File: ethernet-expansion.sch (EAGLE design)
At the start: 22 parts, among them Q1 25MHz, U1 ENC28J60-SO

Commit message: Add center tap connection and interrupt connections
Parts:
- C10, C5, C7, C8, C9: value 100nF -> 0.1uF
- C4, C6: value 0.01uF -> 0.1uF
- R1, R2, R3, R4: value 50 -> 49.9
- R9: value 2K -> 2.32K
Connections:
- net +3V3: now also RJ1.P4
- net ETH_INT0: now also JP1.9
- net ETH_INT1: now also JP1.7
- net GND: now also RJ1.GND

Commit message: Started to route the connector
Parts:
- removed C3: 10uF, resistor:C-EUC0805
- added C11: 10uF, resistor:CPOL-EUE2-4
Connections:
- net GND: now also C11.-, JP1.1; no longer C3.2, JP1.19
- net N$14: now also C11.+; no longer C3.1
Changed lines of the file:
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@@
 <part name="R9" library="resistor" deviceset="R-EU_" device="M0805" value="2.32K"/>
 <part name="GND6" library="supply1" deviceset="GND" device=""/>
-<part name="C3" library="resistor" deviceset="C-EU" device="C0805" value="10uF"/>
 <part name="GND7" library="supply1" deviceset="GND" device=""/>
 <part name="JP1" library="SparkFun-Connectors" deviceset="PINHD-2X10" device=""/>
@@
 <part name="GND14" library="supply1" deviceset="GND" device=""/>
 <part name="GND15" library="supply1" deviceset="GND" device=""/>
+<part name="C11" library="resistor" deviceset="CPOL-EU" device="E2-4" value="10uF"/>
 </parts>
 <sheets>
@@
 <instance part="R9" gate="G$1" x="0" y="43.18" rot="R90"/>
 <instance part="GND6" gate="1" x="0" y="33.02"/>
-<instance part="C3" gate="G$1" x="-12.7" y="45.72"/>
 <instance part="GND7" gate="1" x="-12.7" y="33.02"/>
 <instance part="JP1" gate="A" x="-50.8" y="71.12"/>
 <instance part="+3V4" gate="G$1" x="-27.94" y="58.42" rot="R270"/>
-<instance part="GND8" gate="1" x="-60.96" y="48.26"/>
+<instance part="GND8" gate="1" x="-66.04" y="76.2"/>
 <instance part="RJ1" gate="G$1" x="193.04" y="58.42"/>
 <instance part="GND9" gate="1" x="186.69" y="21.336"/>
@@
 <instance part="GND14" gate="1" x="68.58" y="86.36"/>
 <instance part="GND15" gate="1" x="119.38" y="73.66"/>
+<instance part="C11" gate="G$1" x="-12.7" y="45.72"/>
 </instances>
 <busses>
@@
 </segment>
 <segment>
-<pinref part="C3" gate="G$1" pin="2"/>
 <pinref part="GND7" gate="1" pin="GND"/>
 <wire x1="-12.7" y1="40.64" x2="-12.7" y2="35.56" width="0.1524" layer="91"/>
-</segment>
-<segment>
-<pinref part="JP1" gate="A" pin="19"/>
-<wire x1="-53.34" y1="58.42" x2="-60.96" y2="58.42" width="0.1524" layer="91"/>
-<pinref part="GND8" gate="1" pin="GND"/>
-<wire x1="-60.96" y1="58.42" x2="-60.96" y2="50.8" width="0.1524" layer="91"/>
+<pinref part="C11" gate="G$1" pin="-"/>
 </segment>
 <segment>
@@
 <pinref part="GND15" gate="1" pin="GND"/>
 <wire x1="127" y1="76.2" x2="119.38" y2="76.2" width="0.1524" layer="91"/>
+</segment>
+<segment>
+<pinref part="JP1" gate="A" pin="1"/>
+<pinref part="GND8" gate="1" pin="GND"/>
+<wire x1="-53.34" y1="81.28" x2="-66.04" y2="81.28" width="0.1524" layer="91"/>
+<wire x1="-66.04" y1="81.28" x2="-66.04" y2="78.74" width="0.1524" layer="91"/>
 </segment>
 </net>
@@
 <segment>
 <pinref part="U1" gate="G$1" pin="VCAP"/>
-<pinref part="C3" gate="G$1" pin="1"/>
 <wire x1="2.54" y1="53.34" x2="-12.7" y2="53.34" width="0.1524" layer="91"/>
 <wire x1="-12.7" y1="53.34" x2="-12.7" y2="48.26" width="0.1524" layer="91"/>
-</segment>
-</net>
+<pinref part="C11" gate="G$1" pin="+"/>
+</segment>
+</net>

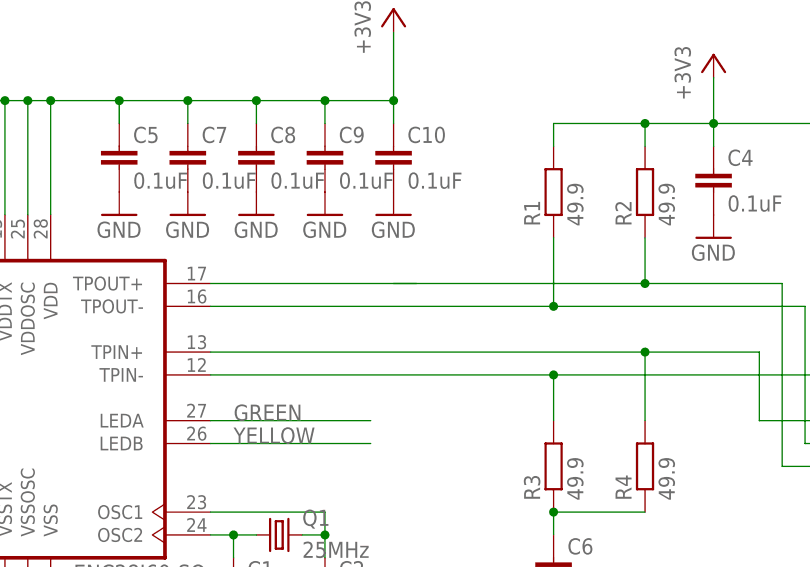
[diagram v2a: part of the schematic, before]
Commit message: Initial board with all wires routed
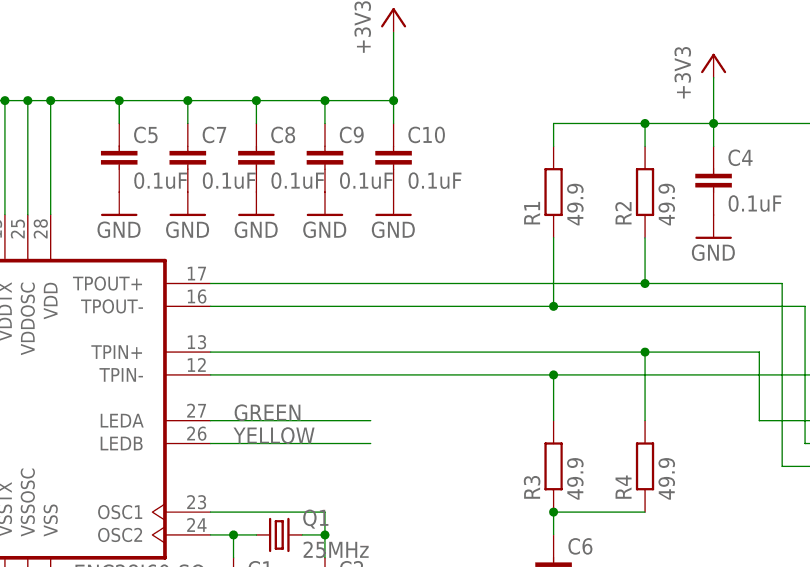
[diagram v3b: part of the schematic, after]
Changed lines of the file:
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@@
-</segment>
-</net>
-<net name="N$7" class="0">
-<segment>
-<wire x1="68.58" y1="78.74" x2="71.12" y2="78.74" width="0.1524" layer="91"/>
 </segment>
 </net>

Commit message: Adding ground fill on top layer and trying out other placements
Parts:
- removed R7: 10K, resistor:R-EU_M0805
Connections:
- removed net N$16: R7.1, U1.RESET
- new net ETH_RESET: JP1.12, U1.RESET
- net +3V3: no longer R7.2
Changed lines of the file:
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@@
 <part name="C2" library="resistor" deviceset="C-EU" device="C0805" value="10pF"/>
 <part name="GND4" library="supply1" deviceset="GND" device=""/>
-<part name="R7" library="resistor" deviceset="R-EU_" device="M0805" value="10K"/>
-<part name="+3V3" library="supply1" deviceset="+3V3" device=""/>
 <part name="C5" library="resistor" deviceset="C-EU" device="C0805" value="0.1uF"/>
 <part name="GND5" library="supply1" deviceset="GND" device=""/>
@@
 <instance part="C2" gate="G$1" x="60.96" y="45.72"/>
 <instance part="GND4" gate="1" x="50.8" y="33.02"/>
-<instance part="R7" gate="G$1" x="0" y="88.9" rot="R90"/>
-<instance part="+3V3" gate="G$1" x="0" y="99.06"/>
 <instance part="C5" gate="G$1" x="38.1" y="93.98"/>
 <instance part="GND5" gate="1" x="38.1" y="86.36"/>
@@
 <pinref part="RJ1" gate="G$1" pin="P4"/>
 <wire x1="116.84" y1="66.04" x2="127" y2="66.04" width="0.1524" layer="91"/>
-</segment>
-<segment>
-<pinref part="R7" gate="G$1" pin="2"/>
-<pinref part="+3V3" gate="G$1" pin="+3V3"/>
-<wire x1="0" y1="93.98" x2="0" y2="96.52" width="0.1524" layer="91"/>
 </segment>
 <segment>
@@
 </segment>
 </net>
-<net name="N$16" class="0">
+<net name="ETH_RESET" class="0">
 <segment>
 <pinref part="U1" gate="G$1" pin="RESET"/>
-<pinref part="R7" gate="G$1" pin="1"/>
-<wire x1="2.54" y1="73.66" x2="0" y2="73.66" width="0.1524" layer="91"/>
-<wire x1="0" y1="73.66" x2="0" y2="83.82" width="0.1524" layer="91"/>
-</segment>
-</net>
+<wire x1="2.54" y1="73.66" x2="-15.24" y2="73.66" width="0.1524" layer="91"/>
+<wire x1="-15.24" y1="73.66" x2="-15.24" y2="55.88" width="0.1524" layer="91"/>
+<wire x1="-15.24" y1="55.88" x2="-35.56" y2="55.88" width="0.1524" layer="91"/>
+<wire x1="-35.56" y1="55.88" x2="-35.56" y2="68.58" width="0.1524" layer="91"/>
+<pinref part="JP1" gate="A" pin="12"/>
+<wire x1="-35.56" y1="68.58" x2="-45.72" y2="68.58" width="0.1524" layer="91"/>
+<label x="-12.7" y="73.66" size="1.778" layer="95"/>
+</segment>
+</net>

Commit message: Routed differential pairs and fixed most of the drc errors
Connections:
- net N$1 renamed TPOUT_P
- net N$2 renamed TPOUT_N
- net N$3 renamed TPIN_P
- net N$4 renamed TPIN_N
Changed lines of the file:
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@@
 <grid distance="0.1" unitdist="inch" unit="inch" style="lines" multiple="1" display="no" altdistance="0.01" altunitdist="inch" altunit="inch"/>
 <layers>
-<layer number="1" name="Top" color="4" fill="1" visible="no" active="no"/>
-<layer number="16" name="Bottom" color="1" fill="1" visible="no" active="no"/>
-<layer number="17" name="Pads" color="2" fill="1" visible="no" active="no"/>
-<layer number="18" name="Vias" color="2" fill="1" visible="no" active="no"/>
-<layer number="19" name="Unrouted" color="6" fill="1" visible="no" active="no"/>
-<layer number="20" name="Dimension" color="15" fill="1" visible="no" active="no"/>
-<layer number="21" name="tPlace" color="7" fill="1" visible="no" active="no"/>
-<layer number="22" name="bPlace" color="7" fill="1" visible="no" active="no"/>
-<layer number="23" name="tOrigins" color="15" fill="1" visible="no" active="no"/>
-<layer number="24" name="bOrigins" color="15" fill="1" visible="no" active="no"/>
-<layer number="25" name="tNames" color="7" fill="1" visible="no" active="no"/>
-<layer number="26" name="bNames" color="7" fill="1" visible="no" active="no"/>
-<layer number="27" name="tValues" color="7" fill="1" visible="no" active="no"/>
-<layer number="28" name="bValues" color="7" fill="1" visible="no" active="no"/>
+<layer number="1" name="Top" color="4" fill="1" visible="yes" active="no"/>
+<layer number="16" name="Bottom" color="1" fill="1" visible="yes" active="no"/>
+<layer number="17" name="Pads" color="2" fill="1" visible="yes" active="no"/>
+<layer number="18" name="Vias" color="2" fill="1" visible="yes" active="no"/>
+<layer number="19" name="Unrouted" color="6" fill="1" visible="yes" active="no"/>
+<layer number="20" name="Dimension" color="15" fill="1" visible="yes" active="no"/>
+<layer number="21" name="tPlace" color="7" fill="1" visible="yes" active="no"/>
+<layer number="22" name="bPlace" color="7" fill="1" visible="yes" active="no"/>
+<layer number="23" name="tOrigins" color="15" fill="1" visible="yes" active="no"/>
+<layer number="24" name="bOrigins" color="15" fill="1" visible="yes" active="no"/>
+<layer number="25" name="tNames" color="7" fill="1" visible="yes" active="no"/>
+<layer number="26" name="bNames" color="7" fill="1" visible="yes" active="no"/>
+<layer number="27" name="tValues" color="7" fill="1" visible="yes" active="no"/>
+<layer number="28" name="bValues" color="7" fill="1" visible="yes" active="no"/>
 <layer number="29" name="tStop" color="7" fill="3" visible="no" active="no"/>
 <layer number="30" name="bStop" color="7" fill="6" visible="no" active="no"/>
@@
 <layer number="35" name="tGlue" color="7" fill="4" visible="no" active="no"/>
 <layer number="36" name="bGlue" color="7" fill="5" visible="no" active="no"/>
-<layer number="37" name="tTest" color="7" fill="1" visible="no" active="no"/>
-<layer number="38" name="bTest" color="7" fill="1" visible="no" active="no"/>
+<layer number="37" name="tTest" color="7" fill="1" visible="yes" active="no"/>
+<layer number="38" name="bTest" color="7" fill="1" visible="yes" active="no"/>
 <layer number="39" name="tKeepout" color="4" fill="11" visible="no" active="no"/>
 <layer number="40" name="bKeepout" color="1" fill="11" visible="no" active="no"/>
@@
 <layer number="44" name="Drills" color="7" fill="1" visible="no" active="no"/>
 <layer number="45" name="Holes" color="7" fill="1" visible="no" active="no"/>
-<layer number="46" name="Milling" color="3" fill="1" visible="no" active="no"/>
-<layer number="47" name="Measures" color="7" fill="1" visible="no" active="no"/>
-<layer number="48" name="Document" color="7" fill="1" visible="no" active="no"/>
-<layer number="49" name="Reference" color="7" fill="1" visible="no" active="no"/>
-<layer number="50" name="dxf" color="7" fill="1" visible="no" active="no"/>
-<layer number="51" name="tDocu" color="7" fill="1" visible="no" active="no"/>
-<layer number="52" name="bDocu" color="7" fill="1" visible="no" active="no"/>
-<layer number="53" name="tGND_GNDA" color="7" fill="9" visible="no" active="no"/>
-<layer number="54" name="bGND_GNDA" color="1" fill="9" visible="no" active="no"/>
-<layer number="56" name="wert" color="7" fill="1" visible="no" active="no"/>
-<layer number="57" name="tCAD" color="7" fill="1" visible="no" active="no"/>
-<layer number="59" name="tCarbon" color="7" fill="1" visible="no" active="no"/>
-<layer number="60" name="bCarbon" color="7" fill="1" visible="no" active="no"/>
+<layer number="46" name="Milling" color="3" fill="1" visible="yes" active="no"/>
+<layer number="47" name="Measures" color="7" fill="1" visible="yes" active="no"/>
+<layer number="48" name="Document" color="7" fill="1" visible="yes" active="no"/>
+<layer number="49" name="Reference" color="7" fill="1" visible="yes" active="no"/>
+<layer number="50" name="dxf" color="7" fill="1" visible="yes" active="no"/>
+<layer number="51" name="tDocu" color="7" fill="1" visible="yes" active="no"/>
+<layer number="52" name="bDocu" color="7" fill="1" visible="yes" active="no"/>
+<layer number="53" name="tGND_GNDA" color="7" fill="9" visible="yes" active="no"/>
+<layer number="54" name="bGND_GNDA" color="1" fill="9" visible="yes" active="no"/>
+<layer number="56" name="wert" color="7" fill="1" visible="yes" active="no"/>
+<layer number="57" name="tCAD" color="7" fill="1" visible="yes" active="no"/>
+<layer number="59" name="tCarbon" color="7" fill="1" visible="yes" active="no"/>
+<layer number="60" name="bCarbon" color="7" fill="1" visible="yes" active="no"/>
 <layer number="90" name="Modules" color="5" fill="1" visible="yes" active="yes"/>
 <layer number="91" name="Nets" color="2" fill="1" visible="yes" active="yes"/>
@@
 </busses>
 <nets>
-<net name="N$1" class="0">
+<net name="TPOUT_P" class="0">
 <segment>
 <pinref part="U1" gate="G$1" pin="TPOUT+"/>
@@
 </segment>
 </net>
-<net name="N$2" class="0">
+<net name="TPOUT_N" class="0">
 <segment>
 <pinref part="U1" gate="G$1" pin="TPOUT-"/>
@@
 </segment>
 </net>
-<net name="N$3" class="0">
+<net name="TPIN_P" class="0">
 <segment>
 <pinref part="U1" gate="G$1" pin="TPIN+"/>
@@
 </segment>
 </net>
-<net name="N$4" class="0">
+<net name="TPIN_N" class="0">
 <segment>
 <pinref part="U1" gate="G$1" pin="TPIN-"/>
